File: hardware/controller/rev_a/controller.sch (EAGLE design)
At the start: 95 parts, among them J1 MODULE_CONTROLLER, J2 DM3AT-SF-PEJM5, J3 U.FL-R-SMT, J4 MICRO_USB_B_HIROSE_ZX62-B-5PA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, J5 MICRO_USB_B_HIROSE_ZX62-B-5PA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, J6 TC2030-JLINK-L, J7 TC2030-JLINK-L, J8 JUMPER-3PTH, Q1 MOSFET-NCHANNELSMD, Q2 NX3008PBK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

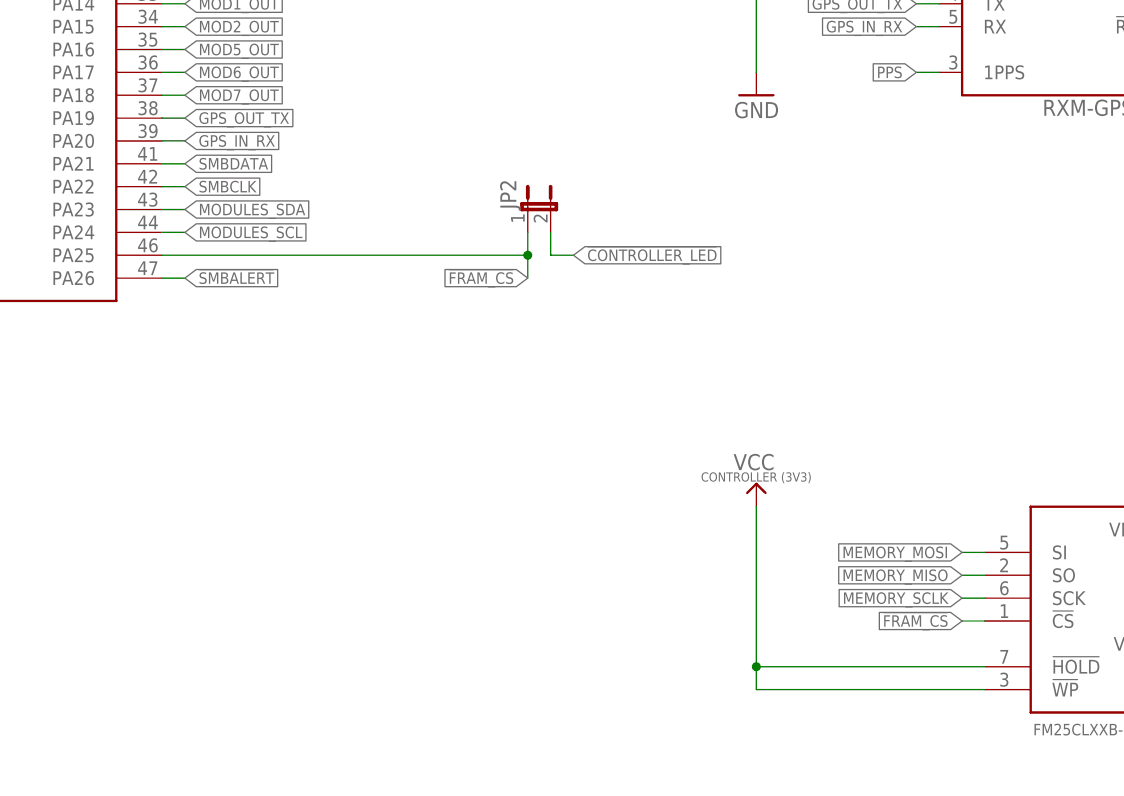
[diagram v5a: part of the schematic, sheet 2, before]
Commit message: Incorporated Brad's comments
 * Removed JP2 (jumper on !FRAM_CS/CONTROLLER_LED)
 * Moved JP1 to top of board
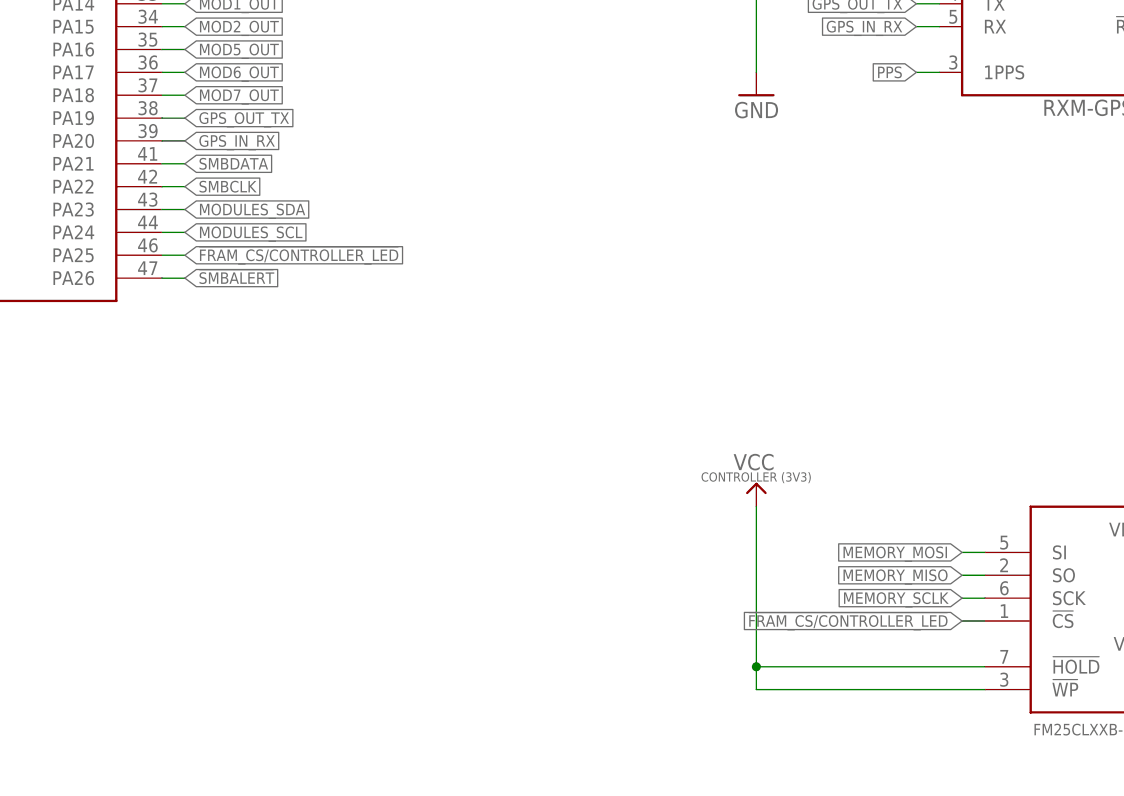
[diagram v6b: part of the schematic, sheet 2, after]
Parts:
- removed JP2: (no value), umich:JUMPER-2PTH
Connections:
- removed net !CONTROLLER_LED: JP2.2, R10.2
- removed net !FRAM_CS: JP2.1, JP3.9, U1.PA25, U4.!CS
- new net !FRAM_CS/CONTROLLER_LED: JP3.9, R10.2, U1.PA25, U4.!CS
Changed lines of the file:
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@@
 <part name="GND34" library="umich" deviceset="GND" device=""/>
 <part name="JP1" library="umich" deviceset="JUMPER-2" device="PTH"/>
-<part name="JP2" library="umich" deviceset="JUMPER-2" device="PTH"/>
 <part name="SJ1" library="SparkFun-Passives" deviceset="SOLDERJUMPER_2WAY" device="PASTE2&amp;3"/>
 <part name="SJ2" library="SparkFun-Passives" deviceset="SOLDERJUMPER" device="TRACE"/>
@@
 </segment>
 </net>
-<net name="!FRAM_CS" class="0">
+<net name="!FRAM_CS/CONTROLLER_LED" class="0">
 <segment>
 <pinref part="JP3" gate="A" pin="9"/>
@@
 </instance>
 <instance part="JP1" gate="A" x="154.94" y="144.78"/>
-<instance part="JP2" gate="A" x="147.32" y="88.9"/>
 </instances>
 <busses>
@@
 </segment>
 </net>
-<net name="!FRAM_CS" class="0">
-<segment>
-<pinref part="U4" gate="U1" pin="!CS"/>
-<wire x1="198.12" y1="43.18" x2="195.58" y2="43.18" width="0.1524" layer="91"/>
-<label x="195.58" y="43.18" size="1.27" layer="95" font="vector" rot="R180" xref="yes"/>
-</segment>
-<segment>
-<pinref part="U1" gate="U1" pin="PA25"/>
-<wire x1="106.68" y1="83.82" x2="147.32" y2="83.82" width="0.1524" layer="91"/>
-<pinref part="JP2" gate="A" pin="1"/>
-<wire x1="147.32" y1="83.82" x2="147.32" y2="86.36" width="0.1524" layer="91"/>
-<wire x1="147.32" y1="83.82" x2="147.32" y2="81.28" width="0.1524" layer="91"/>
-<junction x="147.32" y="83.82"/>
-<label x="147.32" y="81.28" size="1.27" layer="95" rot="R180" xref="yes"/>
-</segment>
-</net>
 <net name="SMBDATA" class="0">
 <segment>
@@
 </segment>
 </net>
-<net name="!CONTROLLER_LED" class="0">
-<segment>
-<pinref part="JP2" gate="A" pin="2"/>
-<wire x1="149.86" y1="86.36" x2="149.86" y2="83.82" width="0.1524" layer="91"/>
-<wire x1="149.86" y1="83.82" x2="152.4" y2="83.82" width="0.1524" layer="91"/>
-<label x="152.4" y="83.82" size="1.27" layer="95" xref="yes"/>
+<net name="!FRAM_CS/CONTROLLER_LED" class="0">
+<segment>
+<pinref part="U1" gate="U1" pin="PA25"/>
+<wire x1="106.68" y1="83.82" x2="109.22" y2="83.82" width="0.1524" layer="91"/>
+<label x="109.22" y="83.82" size="1.27" layer="95" xref="yes"/>
+</segment>
+<segment>
+<pinref part="U4" gate="U1" pin="!CS"/>
+<wire x1="198.12" y1="43.18" x2="195.58" y2="43.18" width="0.1524" layer="91"/>
+<label x="195.58" y="43.18" size="1.27" layer="95" font="vector" rot="R180" xref="yes"/>
 </segment>
 </net>
@@
 </segment>
 </net>
-<net name="!CONTROLLER_LED" class="0">
+<net name="!FRAM_CS/CONTROLLER_LED" class="0">
 <segment>
 <pinref part="R10" gate="G$1" pin="2"/>

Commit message: Update digikey part for fram chip
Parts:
- U4: DIGIKEY 428-3206-ND -> FM25CL64B-DGRA-ND
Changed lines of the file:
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@@
 <part name="U3" library="chips" deviceset="RXM-GPS-RM-T" device=""/>
 <part name="U4" library="chips" deviceset="FM25" device="CLXXB-DG" value="FM25CLXXB-DG">
-<attribute name="DIGIKEY" value="428-3206-ND"/>
+<attribute name="DIGIKEY" value="FM25CL64B-DGRA-ND"/>
 </part>
 <part name="J2" library="connector" deviceset="DM3AT-SF-PEJM5" device=""/>

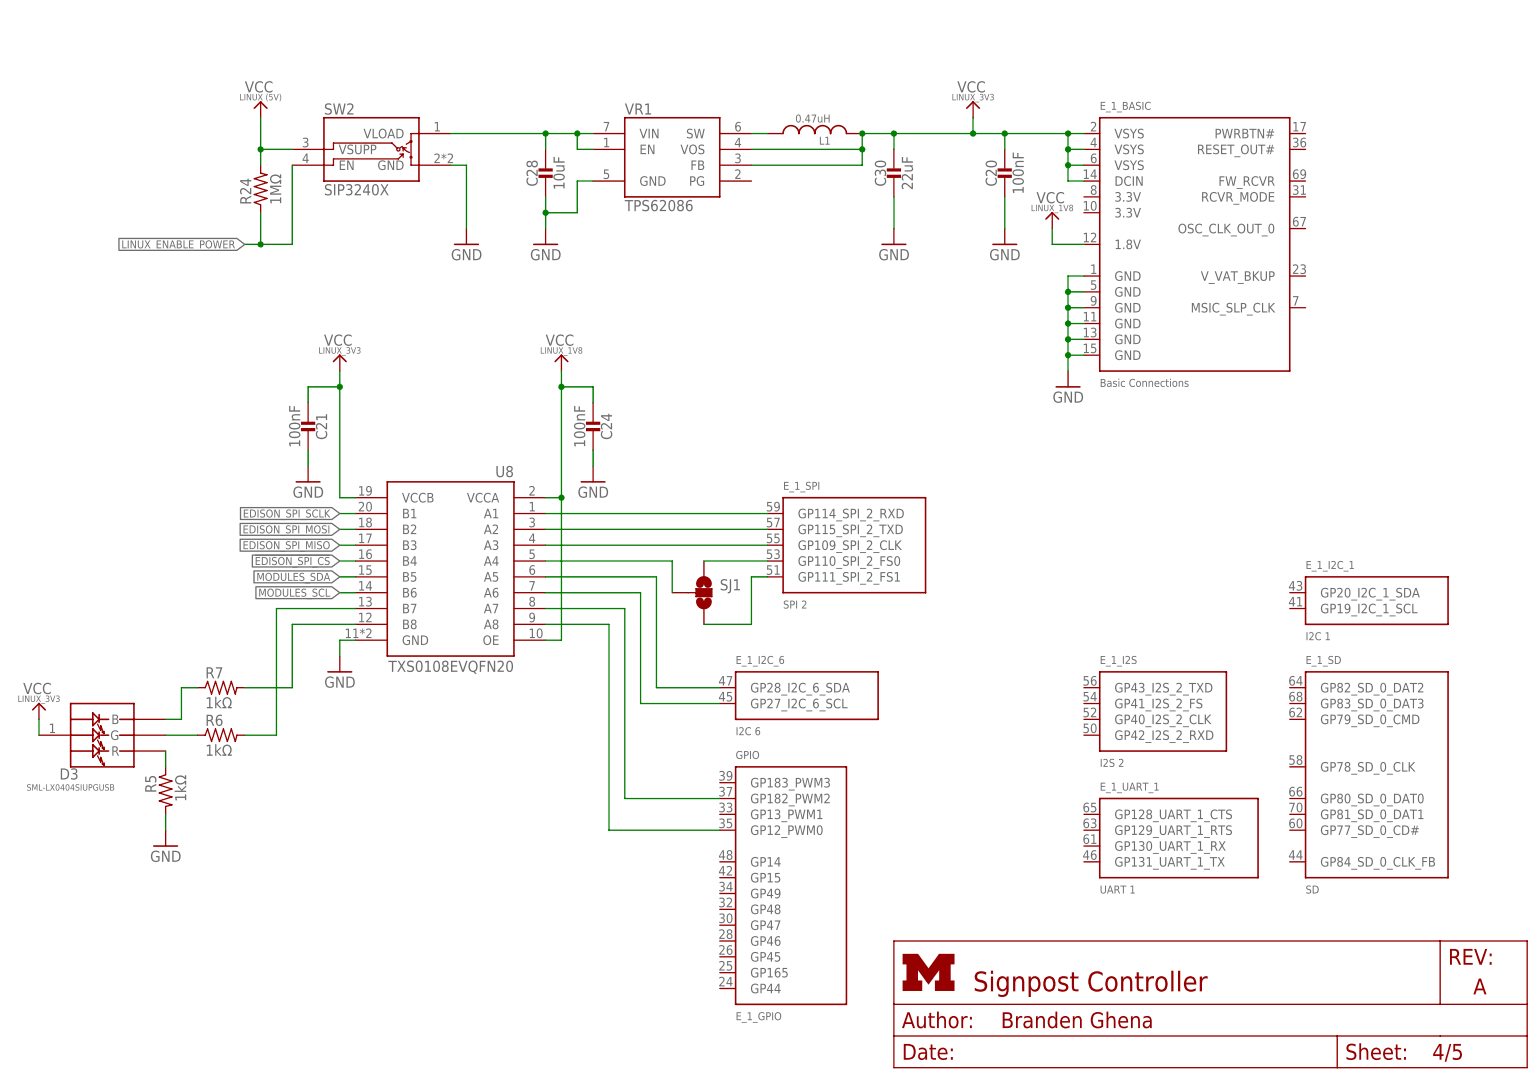
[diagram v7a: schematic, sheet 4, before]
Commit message: Updates to controller
 * Connected Edison PWRBTN# to Storage Master
 * Better silkscreen labels everywhere
 * Added mounting holes
 * Jumper for Edison power to measure current
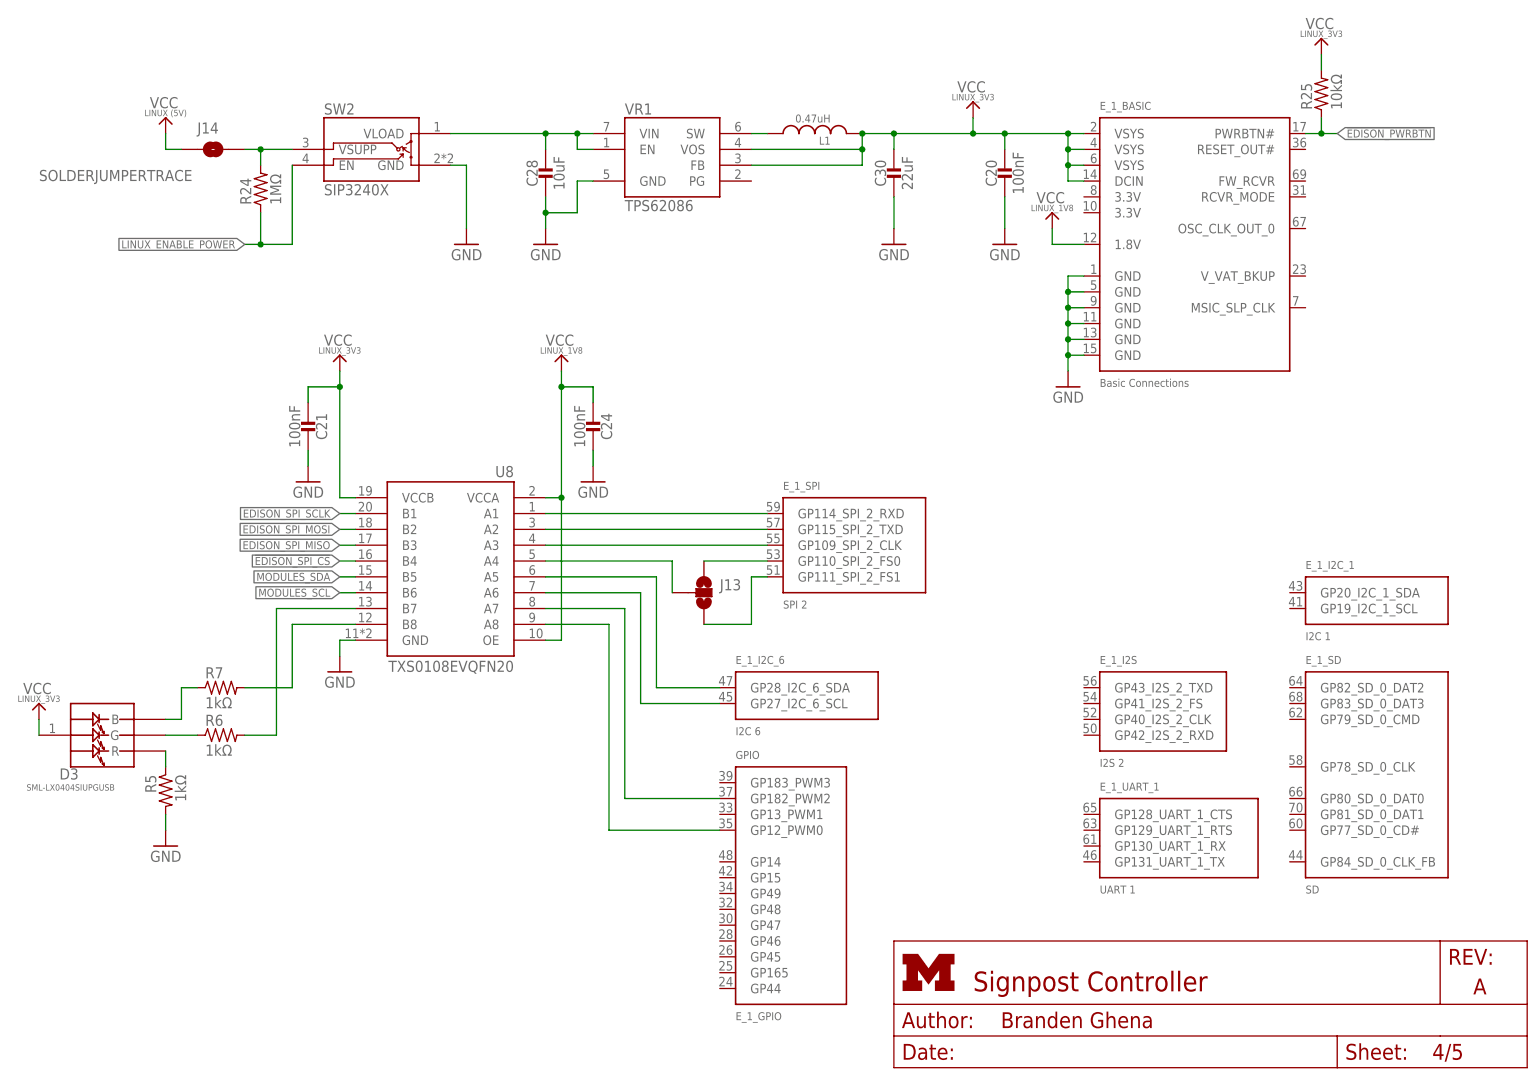
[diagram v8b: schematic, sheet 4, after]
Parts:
- added J14: SOLDERJUMPERTRACE, SparkFun-Passives:SOLDERJUMPERTRACE
- added R25: 10kΩ, passives:RESISTOR0402_RES
- renumbered JP1 to J9, JP3 to J10, JP4 to J11, JP5 to J12, SJ1 to J13, SJ2 to J15
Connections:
- new net !EDISON_PWRBTN: E_1_BASIC.PWRBTN#, R25.1, U2.PA05
- new net N$18: J14.2, R24.2, SW2.VSUPP
- net VCC_LINUX: now also J14.1; no longer R24.2, SW2.VSUPP
- net VCC_LINUX_3V3: now also R25.2
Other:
- note added: "Cut to measure current draw"
